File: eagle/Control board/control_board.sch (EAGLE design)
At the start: 224 parts, among them Q1 RE1C002UN, Q2 RE1C002UN, SW1 SPST_TACT-EVQQ2, SW2 SPST_TACT-EVQQ2, U1 TCA9554A, U2 AZ1085CD, U4 STM32F446, U5 TCA9554A, U6 TCA9554A, U7 AZ1085CD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

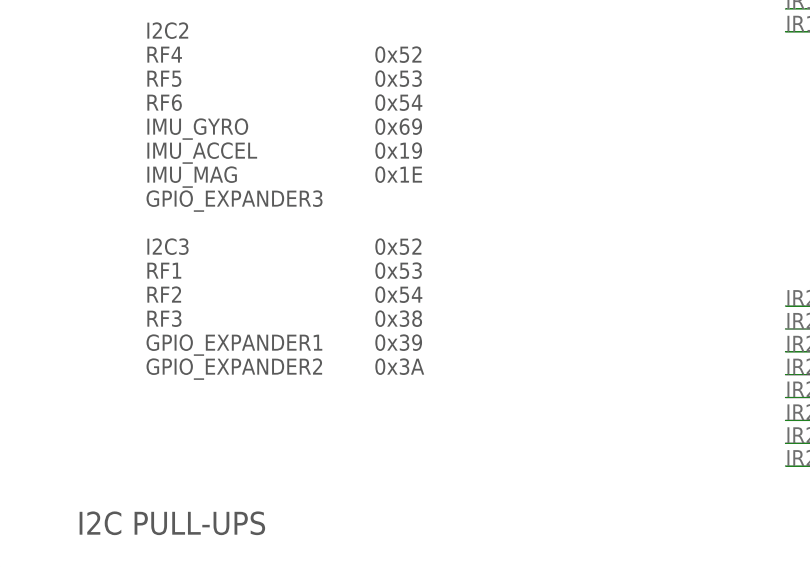
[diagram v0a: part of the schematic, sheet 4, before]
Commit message: Changed .ioc to switch sw1-4 to outputs
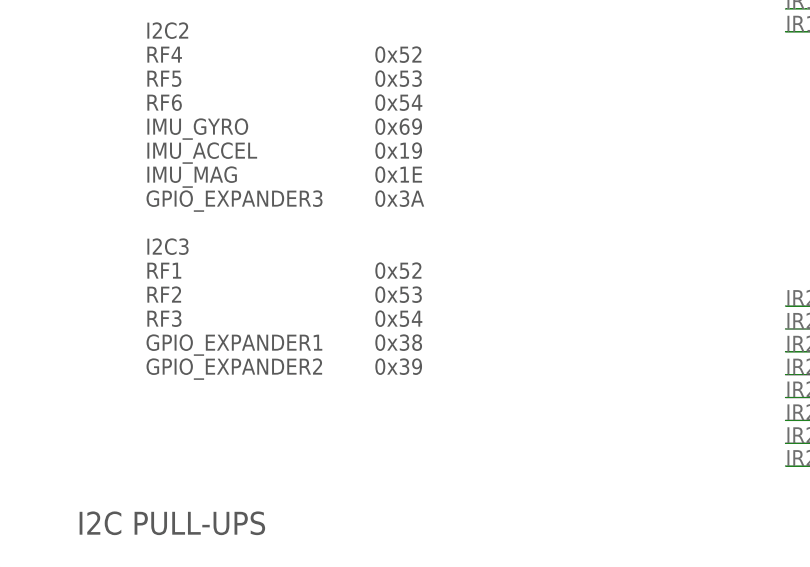
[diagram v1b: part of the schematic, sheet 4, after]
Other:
- note added: "0x52 0x52 0x53 0x54 0x69 0x19 0x1E 0x3A 0x52 0x53 0x54 0x38 0x39"
- note removed: "0x52 0x52 0x53 0x54 0x69 0x19 0x1E 0x52 0x53 0x54 0x38 0x39 0x3A"
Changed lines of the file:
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@@
 0x19
 0x1E
+0x3A
 0x52
 0x53
 0x54
 0x38
-0x39
-0x3A</text>
+0x39</text>
 <text x="114.3" y="45.72" size="2.54" layer="97">I2C PULL-UPS</text>
 </plain>
